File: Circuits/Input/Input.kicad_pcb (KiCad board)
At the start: 2 copper layers, 28.9 x 68.9 mm, 7 parts, among them CN1 WRITER, U1 TWE-Lite_SMD

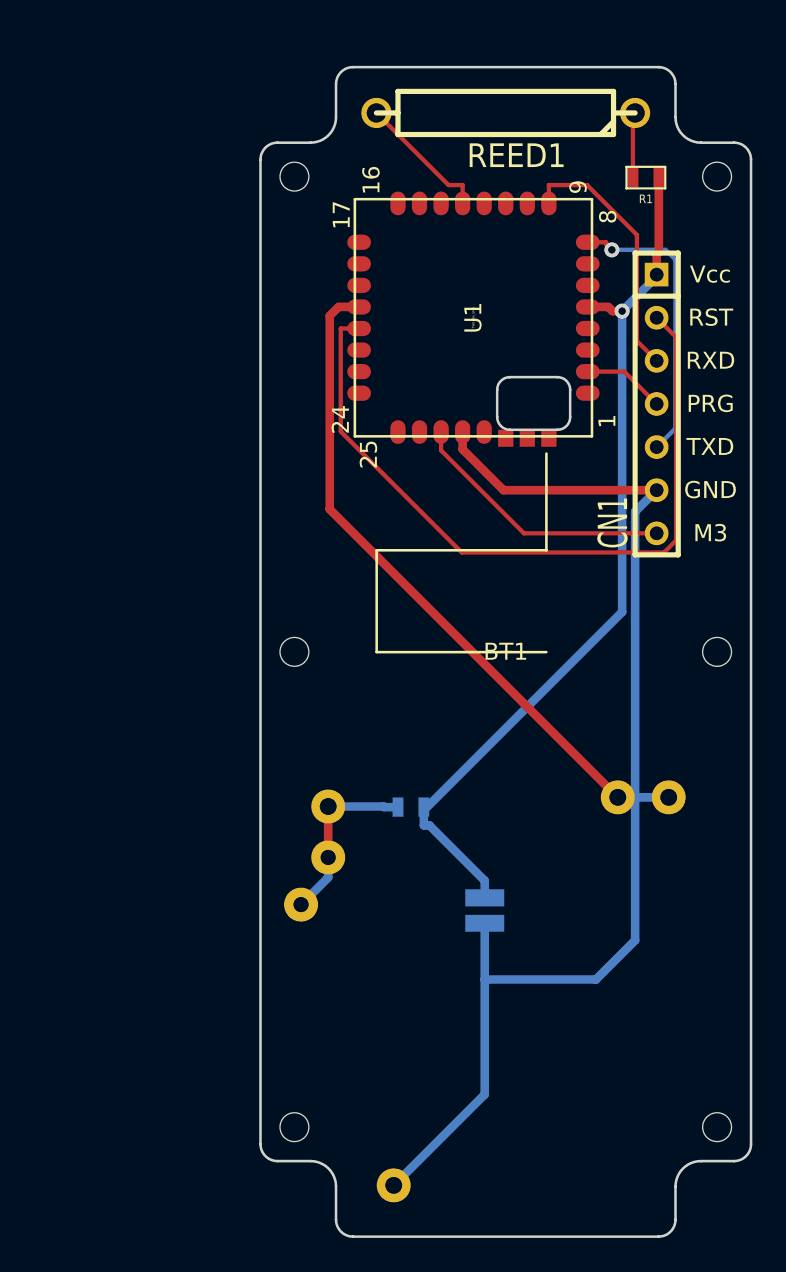
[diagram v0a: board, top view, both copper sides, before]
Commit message: Fixed: Reed switch was not connected to GND.
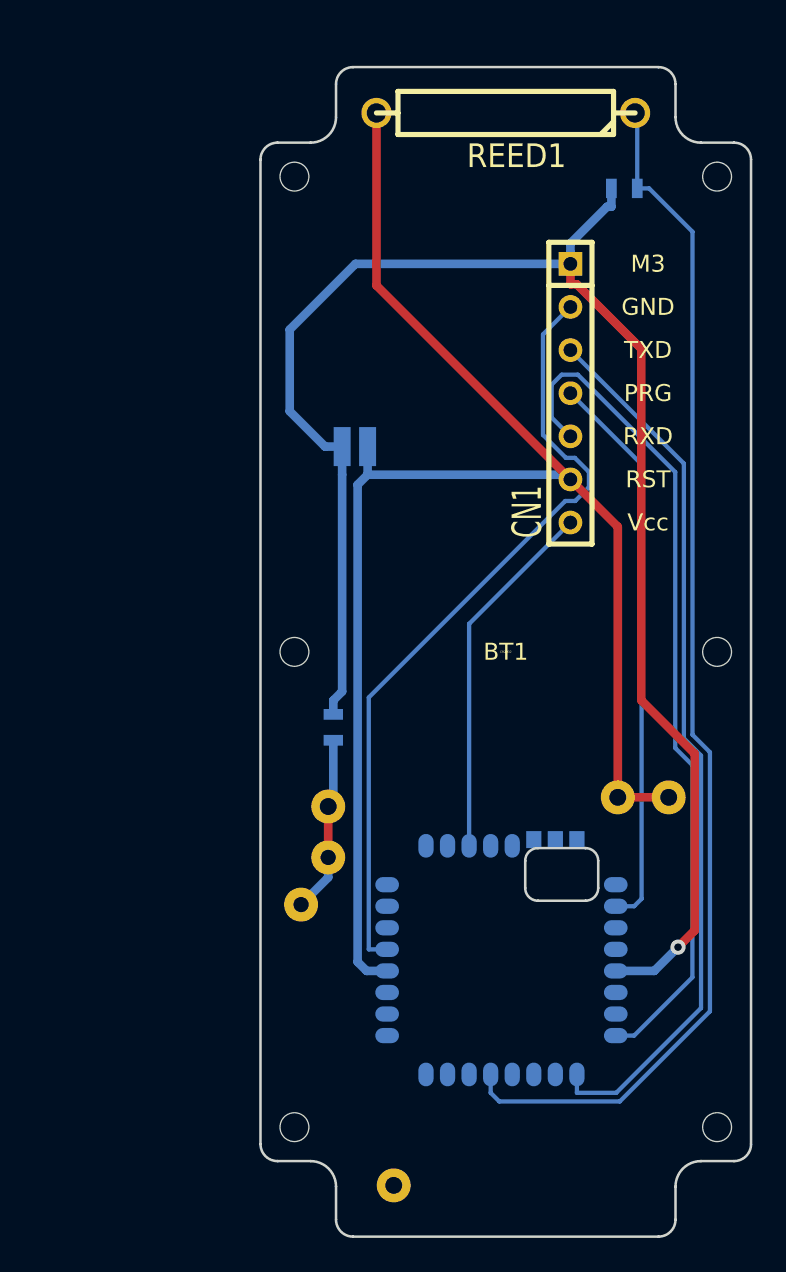
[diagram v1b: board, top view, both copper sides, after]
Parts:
- CN1: footprint SIL-7 -> 2211R-07G-LP
- R1, U1: moved to B.Cu
- moved U1 37.9 mm to (41.7, 69.0), turned to 270 degrees
- moved C1 34.8 mm to (33.0, 33.7), turned to 180 degrees
- moved R2 6.56 mm to (31.8, 55.2), turned to 90 degrees
- moved CN1 5.12 mm to (45.7, 35.6)
- moved R1 1.42 mm to (48.9, 23.5), turned to 180 degrees
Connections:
- R1 pad 1: /PULLUP -> /DOOR
- REED1 pad 1: /PULLUP -> /DOOR
- REED1 pad 2: /DOOR -> GND
- U1 pad 28: GND -> (no net)
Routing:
- net /DOOR: track 7.92 -> 71.6 mm
- net VCC: track 52.3 -> 96.7 mm
- net /RX: track 15.4 -> 52.4 mm
- net /TX: track 17.1 -> 49.5 mm, vias 1 -> 0
- net /PRG: track 4.85 -> 33.2 mm
- net GND: track 108.3 -> 93.8 mm
- net /CFG: track 15.8 -> 21.5 mm
- net /PULLUP: track 3.86 -> 0.00 mm
- net /RST: track 43.7 -> 46.7 mm

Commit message: Set inhibit area under CR2032.
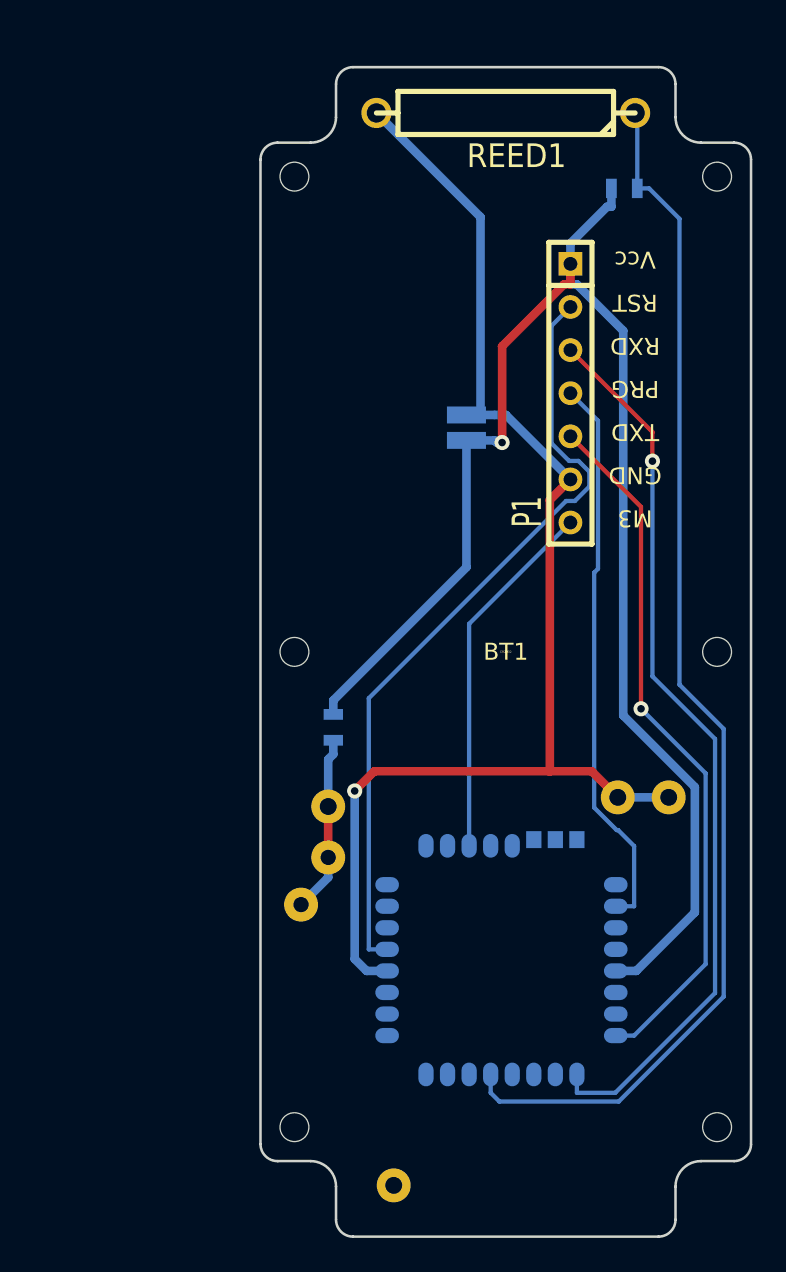
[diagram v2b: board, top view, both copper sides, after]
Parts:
- removed CN1: WRITER, 2211R-07G-LP
- added P1: WRITER-VCC, 2211R-07G-LP, F.Cu at (45.7, 35.6)
- U1: footprint TWE-001L-SMD -> TWE-001L-SMD-noNTH
- moved C1 4.22 mm to (34.5, 37.6), turned to 270 degrees
- turned U1 to 180 degrees
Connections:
- U1 pad 8: /TX -> /TXD
- U1 pad 9: /RX -> /RXD
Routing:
- net /RXD: track 0.00 -> 53.1 mm, vias 0 -> 1
- net /RX: track 52.4 -> 0.00 mm
- net /TX: track 49.5 -> 0.00 mm
- net /TXD: track 0.00 -> 41.4 mm, vias 0 -> 1
- net GND: track 93.8 -> 77.4 mm, vias 0 -> 1
- net VCC: track 96.7 -> 87.1 mm
- net /DOOR: track 71.6 -> 72.2 mm

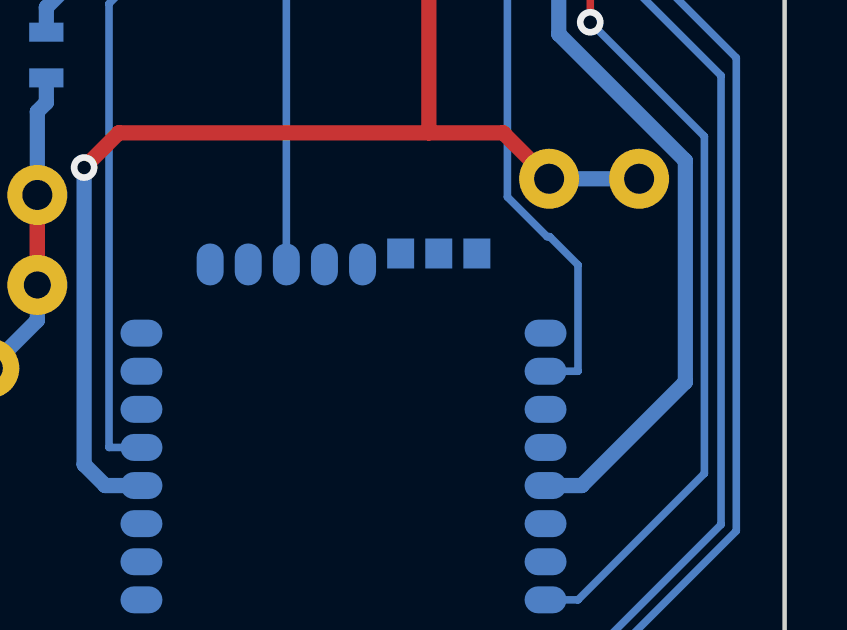
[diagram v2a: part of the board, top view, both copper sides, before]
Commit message: Replaced footprint of TWE-Lite SMD with antenna hole.
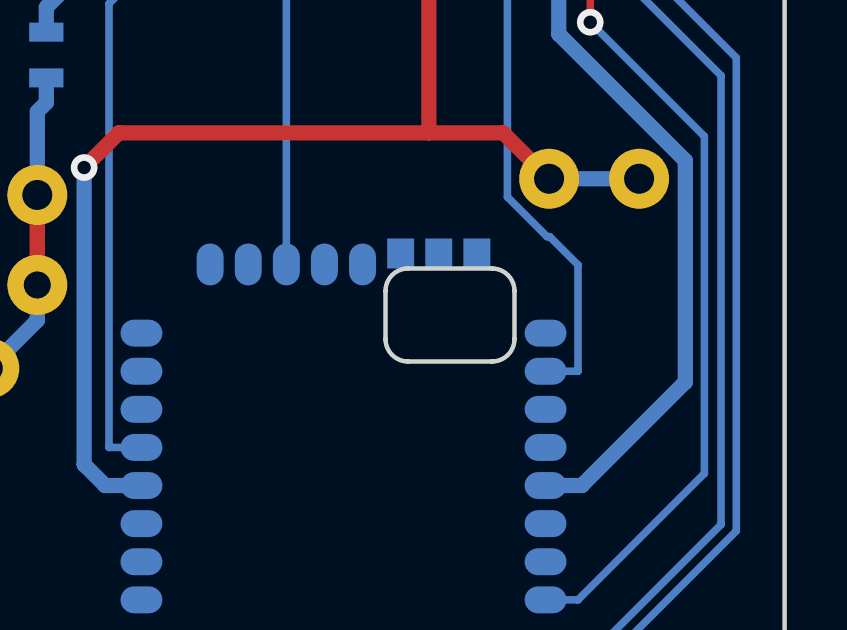
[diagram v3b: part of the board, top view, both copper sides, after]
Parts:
- U1: footprint TWE-001L-SMD-noNTH -> TWE-001L-SMD

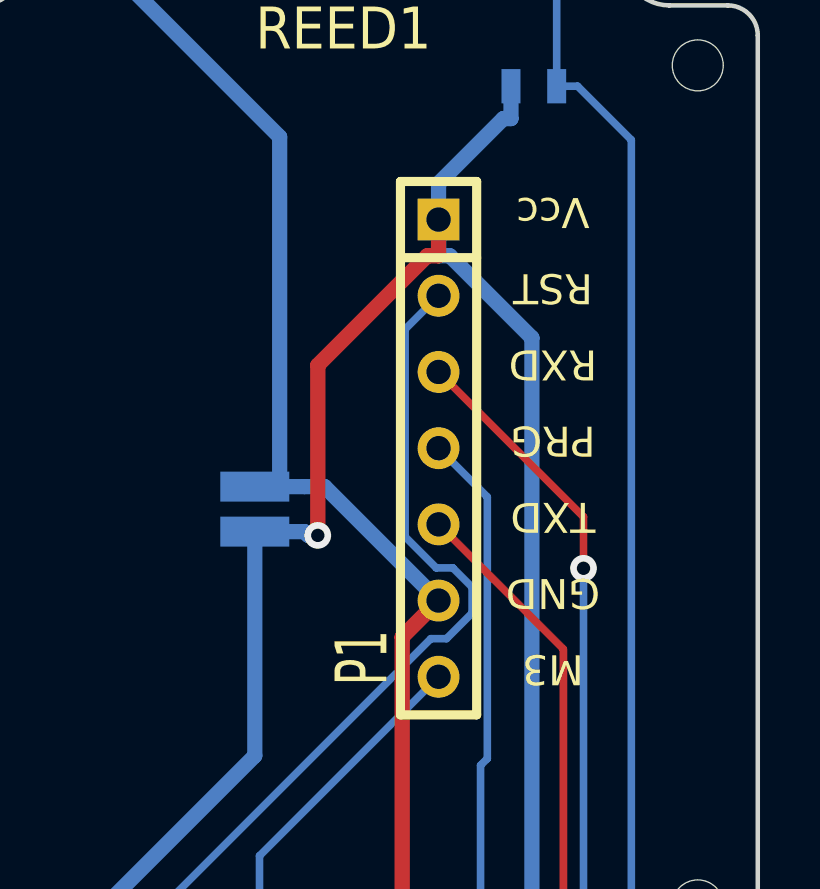
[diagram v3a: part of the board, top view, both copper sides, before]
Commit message: Moved silk position.
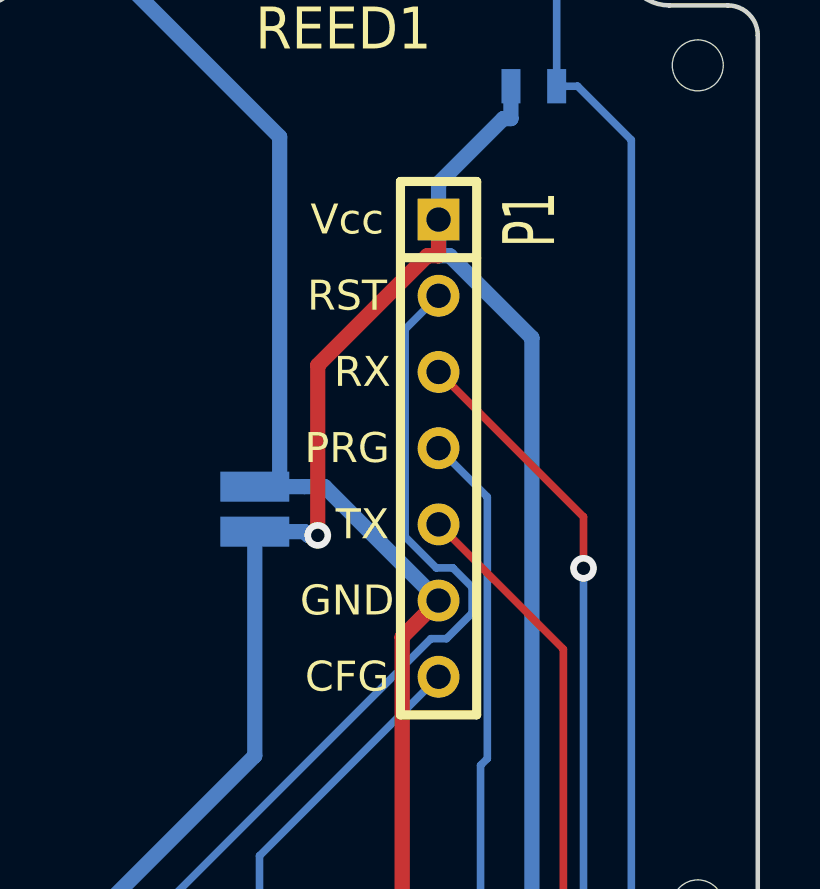
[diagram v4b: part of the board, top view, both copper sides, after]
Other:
- board text added: "CFG"
- board text added: "RX"
- board text added: "TX"
- board text removed: "M3"
- board text removed: "RXD"
- board text removed: "TXD"
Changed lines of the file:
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@@
     (descr "Connecteur 7 pins")
     (tags "CONN DEV")
-    (fp_text reference P1 (at 6.985 2.54 270) (layer F.SilkS)
+    (fp_text reference P1 (at -7.62 -3.048 270) (layer F.SilkS)
       (effects (font (size 1.72974 1.08712) (thickness 0.27178)))
     )
@@
   )
   (target plus (at 25.654 15.494) (size 0.005) (width 0.1) (layer Edge.Cuts))
-  (gr_text M3 (at 49.53 42.926 180) (layer F.SilkS)
-    (effects (font (size 1 1) (thickness 0.2)))
-  )
-  (gr_text TXD (at 49.53 37.846 180) (layer F.SilkS)
-    (effects (font (size 1 1) (thickness 0.2)))
-  )
-  (gr_text PRG (at 49.53 35.306 180) (layer F.SilkS)
-    (effects (font (size 1 1) (thickness 0.2)))
-  )
-  (gr_text RXD (at 49.53 32.766 180) (layer F.SilkS)
-    (effects (font (size 1 1) (thickness 0.2)))
-  )
-  (gr_text RST (at 49.53 30.226 180) (layer F.SilkS)
-    (effects (font (size 1 1) (thickness 0.2)))
-  )
-  (gr_text GND (at 49.53 40.386 180) (layer F.SilkS)
-    (effects (font (size 1 1) (thickness 0.2)))
-  )
-  (gr_text Vcc (at 49.53 27.686 180) (layer F.SilkS)
-    (effects (font (size 1 1) (thickness 0.2)))
-  )
+  (gr_text CFG (at 42.672 43.18) (layer F.SilkS)
+    (effects (font (size 1 1) (thickness 0.2)))
+  )
+  (gr_text TX (at 43.18 38.1) (layer F.SilkS)
+    (effects (font (size 1 1) (thickness 0.2)))
+  )
+  (gr_text PRG (at 42.672 35.56) (layer F.SilkS)
+    (effects (font (size 1 1) (thickness 0.2)))
+  )
+  (gr_text RX (at 43.18 33.02) (layer F.SilkS)
+    (effects (font (size 1 1) (thickness 0.2)))
+  )
+  (gr_text RST (at 42.672 30.48) (layer F.SilkS)
+    (effects (font (size 1 1) (thickness 0.2)))
+  )
+  (gr_text GND (at 42.672 40.64) (layer F.SilkS)
+    (effects (font (size 1 1) (thickness 0.2)))
+  )
+  (gr_text Vcc (at 42.672 27.94) (layer F.SilkS)
+    (effects (font (size 1 1) (thickness 0.2)))
+  )

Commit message: Ordered to PCB prototyping service.
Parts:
- moved R1 13.4 mm to (35.6, 21.6)
- moved R2 13.4 mm to (18.5, 53.4)
- moved U1 13.4 mm to (28.4, 67.1)
- moved BT1 13.4 mm to (28.6, 48.9)
- moved C1 13.4 mm to (21.3, 35.7)
- moved P1 13.4 mm to (32.4, 33.7)
- moved REED1 13.4 mm to (28.6, 17.2)
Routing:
- added copper zone on F.Cu, net (none)
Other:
- outline, holes or cut-outs redrawn
- board text added: "DoorChecker Input"
